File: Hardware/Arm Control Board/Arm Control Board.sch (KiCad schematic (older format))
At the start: 12 parts

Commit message: Added new AP65552SP-13 regulator circuit
More current for the servos
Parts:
- removed 100, C?: CP1, symbol CP1
- removed 3k: R, symbol R
- removed C?: 470 pF, symbol C
- removed D?: 1N5819, symbol DIODESCH
- removed L?: 220 uH, symbol INDUCTOR_SMALL
- removed R?: 1k, symbol R
- removed R?: .33???, symbol R
- removed U?: AZ34063UMTR-G1, symbol AZ34063UMTR-G1
- added C? (x2): 10uF, symbol C
- added C?: .1uF, symbol C
- added C? (x2): 22uF, symbol C
- added C?: 8.2nF, symbol C
- added C?: 1uF, symbol C
- added C?: 18pF, symbol C
- added L?: 3.3uH, symbol INDUCTOR_SMALL
- added P?: BATT, symbol BATT
- added R?: 100K, symbol R
- added R?: 22.1K, symbol R
- added R?: 8.25K, symbol R
- added U?: AP65552SP-13, symbol AP65552SP-13
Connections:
- wire segments 32 -> 38
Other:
- moved on the sheet: P?

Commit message: Creating servo regulator circuits, datasheets
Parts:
- added C? (x2): 10uF, symbol C
- added C?: .1uF, symbol C
- added C? (x2): 22uF, symbol C
- added C?: 8.2nF, symbol C
- added C?: 1uF, symbol C
- added C?: 18pF, symbol C
- added L?: 3.3uH, symbol INDUCTOR_SMALL
- added R?: 100K, symbol R
- added R?: 22.1K, symbol R
- added R?: 8.25K, symbol R
- added U?: AP65552SP-13, symbol AP65552SP-13
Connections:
- wire segments 38 -> 84
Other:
- moved on the sheet: C?, L?, R?, U?

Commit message: Added enable pins to all servo regulators
Might not need them all independent, we'll see
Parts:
- removed C? (x4): 10uF, symbol C
- removed C? (x2): .1uF, symbol C
- removed C? (x4): 22uF, symbol C
- removed C? (x2): 8.2nF, symbol C
- removed C? (x2): 1uF, symbol C
- removed C? (x2): 18pF, symbol C
- removed L? (x2): 3.3uH, symbol INDUCTOR_SMALL
- removed R? (x2): 100K, symbol R
- removed R? (x2): 22.1K, symbol R
- removed R? (x2): 8.25K, symbol R
- removed U? (x2): AP65552SP-13, symbol AP65552SP-13
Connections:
- wire segments 84 -> 8

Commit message: Added and connected servo plugs
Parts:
- added P? (x5): SERVO, symbol SERVO
- added U? (x2): STM32F410RCT6, symbol STM32F410RCT6
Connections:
- wire segments 8 -> 52
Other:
- moved on the sheet: P?, U?A

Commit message: Added lower cost 485 Transceiver, connected serial
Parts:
- removed U?: ST485CDR, symbol ST485CDR
- added U?: SN75176BDR, symbol SN75176BDR
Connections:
- wire segments 52 -> 63
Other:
- moved on the sheet: P?
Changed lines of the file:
@@
-$EndComp
-$Comp
-L ST485CDR U?
-U 1 1 54C4799F
-P 8100 1000
-F 0 "U?" H 7950 550 60  0000 C CNN
-F 1 "ST485CDR" H 7900 1150 60  0000 C CNN
-F 2 "" H 8100 1000 60  0000 C CNN
-F 3 "" H 8100 1000 60  0000 C CNN
-	1    8100 1000
-	1    0    0    -1
 $EndComp
 $Comp
 L RS485 P?
 U 1 1 54C47C8E
-P 9100 1150
-F 0 "P?" H 9100 1300 50  0000 C CNN
-F 1 "RS485" V 9200 1150 50  0000 C CNN
-F 2 "" H 9100 1150 60  0000 C CNN
-F 3 "" H 9100 1150 60  0000 C CNN
-	1    9100 1150
+P 4100 1450
+F 0 "P?" H 4100 1600 50  0000 C CNN
+F 1 "RS485" V 4200 1450 50  0000 C CNN
+F 2 "" H 4100 1450 60  0000 C CNN
+F 3 "" H 4100 1450 60  0000 C CNN
+	1    4100 1450
 	1    0    0    -1
 $EndComp
@@
 L GND #PWR01
 U 1 1 54C47E58
-P 8500 1500
-F 0 "#PWR01" H 8500 1250 60  0001 C CNN
-F 1 "GND" H 8500 1350 60  0000 C CNN
-F 2 "" H 8500 1500 60  0000 C CNN
-F 3 "" H 8500 1500 60  0000 C CNN
-	1    8500 1500
-	1    0    0    -1
-$EndComp
-Wire Wire Line
-	8900 1100 8300 1100
-Wire Wire Line
-	8300 1200 8900 1200
-Wire Wire Line
-	8300 1300 8500 1300
-Wire Wire Line
-	8500 1300 8500 1500
+P 3500 1800
+F 0 "#PWR01" H 3500 1550 60  0001 C CNN
+F 1 "GND" H 3500 1650 60  0000 C CNN
+F 2 "" H 3500 1800 60  0000 C CNN
+F 3 "" H 3500 1800 60  0000 C CNN
+	1    3500 1800
+	1    0    0    -1
+$EndComp
 $Comp
 L BATT P?
@@
 	1    0    0    -1
 $EndComp
-Wire Wire Line
-	850  750  950  750
-Wire Wire Line
-	950  750  950  850
-Wire Wire Line
-	850  650  1200 650
-Wire Wire Line
-	1200 650  1200 850
 $Sheet
 S 4900 3150 1650 1950
@@
 	-1   0    0    1
 $EndComp
-Wire Wire Line
-	4900 3250 2350 3250
-Wire Wire Line
-	4900 3400 4300 3400
-Wire Wire Line
-	4300 3400 4300 3900
-Wire Wire Line
-	4300 3900 2350 3900
-Wire Wire Line
-	4450 3550 4450 4600
-Wire Wire Line
-	4450 4600 2350 4600
-Wire Wire Line
-	4450 3550 4900 3550
-Wire Wire Line
-	4900 3700 4600 3700
-Wire Wire Line
-	4600 3700 4600 5300
-Wire Wire Line
-	4600 5300 2350 5300
-Wire Wire Line
-	4900 3850 4750 3850
-Wire Wire Line
-	4750 3850 4750 6000
-Wire Wire Line
-	4750 6000 2350 6000
 $Comp
 L GND #PWR?
@@
 	1    0    0    -1
 $EndComp
-Wire Wire Line
-	2350 3350 2500 3350
-Wire Wire Line
-	2500 3350 2500 3450
 $Comp
 L GND #PWR?
@@
 	1    0    0    -1
 $EndComp
-Wire Wire Line
-	2350 4000 2500 4000
-Wire Wire Line
-	2500 4000 2500 4100
 $Comp
 L GND #PWR?
@@
 	1    0    0    -1
 $EndComp
-Wire Wire Line
-	2350 4700 2500 4700
-Wire Wire Line
-	2500 4700 2500 4800
 $Comp
 L GND #PWR?
@@
 	1    0    0    -1
 $EndComp
-Wire Wire Line
-	2500 5400 2500 5500
 $Comp
 L GND #PWR?
@@
 	1    0    0    -1
 $EndComp
-Wire Wire Line
-	2350 6100 2500 6100
-Wire Wire Line
-	2500 6100 2500 6200
-Wire Wire Line
-	2500 5400 2350 5400
-Wire Wire Line
-	1400 1850 2650 1850
-Wire Wire Line
-	2650 1850 2650 3150
-Wire Wire Line
-	2650 3150 2350 3150
-Wire Wire Line
-	1400 1950 2750 1950
-Wire Wire Line
-	2750 1950 2750 3800
-Wire Wire Line
-	2750 3800 2350 3800
 $Comp
 L STM32F410RCT6 U?
@@
 	1    0    0    -1
 $EndComp
-Wire Wire Line
-	1400 3000 1900 3000
-Wire Wire Line
-	1900 3000 1900 4400
-Wire Wire Line
-	1900 4400 2500 4400
-Wire Wire Line
-	2500 4400 2500 4500
-Wire Wire Line
-	2500 4500 2350 4500
 $Comp
 L STM32F410RCT6 U?
@@
 $EndComp
 Wire Wire Line
+	3900 1400 3300 1400
+Wire Wire Line
+	3300 1500 3900 1500
+Wire Wire Line
+	3300 1600 3500 1600
+Wire Wire Line
+	3500 1600 3500 1800
+Wire Wire Line
+	850  750  950  750
+Wire Wire Line
+	950  750  950  850
+Wire Wire Line
+	850  650  1200 650
+Wire Wire Line
+	1200 650  1200 850
+Wire Wire Line
+	4900 3250 2350 3250
+Wire Wire Line
+	4900 3400 4300 3400
+Wire Wire Line
+	4300 3400 4300 3900
+Wire Wire Line
+	4300 3900 2350 3900
+Wire Wire Line
+	4450 3550 4450 4600
+Wire Wire Line
+	4450 4600 2350 4600
+Wire Wire Line
+	4450 3550 4900 3550
+Wire Wire Line
+	4900 3700 4600 3700
+Wire Wire Line
+	4600 3700 4600 5300
+Wire Wire Line
+	4600 5300 2350 5300
+Wire Wire Line
+	4900 3850 4750 3850
+Wire Wire Line
+	4750 3850 4750 6000
+Wire Wire Line
+	4750 6000 2350 6000
+Wire Wire Line
+	2350 3350 2500 3350
+Wire Wire Line
+	2500 3350 2500 3450
+Wire Wire Line
+	2350 4000 2500 4000
+Wire Wire Line
+	2500 4000 2500 4100
+Wire Wire Line
+	2350 4700 2500 4700
+Wire Wire Line
+	2500 4700 2500 4800
+Wire Wire Line
+	2500 5400 2500 5500
+Wire Wire Line
+	2350 6100 2500 6100
+Wire Wire Line
+	2500 6100 2500 6200
+Wire Wire Line
+	2500 5400 2350 5400
+Wire Wire Line
+	1400 1850 2650 1850
+Wire Wire Line
+	2650 1850 2650 3150
+Wire Wire Line
+	2650 3150 2350 3150
+Wire Wire Line
+	1400 1950 2750 1950
+Wire Wire Line
+	2750 1950 2750 3800
+Wire Wire Line
+	2750 3800 2350 3800
+Wire Wire Line
+	1400 3000 1900 3000
+Wire Wire Line
+	1900 3000 1900 4400
+Wire Wire Line
+	1900 4400 2500 4400
+Wire Wire Line
+	2500 4400 2500 4500
+Wire Wire Line
+	2500 4500 2350 4500
+Wire Wire Line
 	1400 5550 1900 5550
 Wire Wire Line
@@
 Wire Wire Line
 	2500 5900 2350 5900
+Wire Notes Line
+	7150 6750 7150 6800
+Wire Notes Line
+	7150 6800 7450 6800
+Wire Notes Line
+	7450 6800 7450 6750
+Wire Notes Line
+	7450 6750 7150 6750
+Wire Notes Line
+	7300 6750 7300 6700
+Wire Notes Line
+	7250 6700 7350 6700
+Wire Notes Line
+	7250 6700 7250 6650
+Wire Notes Line
+	7250 6650 7350 6650
+Wire Notes Line
+	7350 6650 7350 6700
+Wire Notes Line
+	7150 6850 7300 6800
+Wire Notes Line
+	7150 6850 7100 6850
+Wire Notes Line
+	7150 6850 7150 6900
+Wire Notes Line
+	7150 6900 7100 6900
+Wire Notes Line
+	7100 6900 7100 6850
+Wire Notes Line
+	7500 6850 7450 6850
+Wire Notes Line
+	7450 6850 7450 6900
+Wire Notes Line
+	7450 6900 7500 6900
+Wire Notes Line
+	7500 6900 7500 6850
+Wire Notes Line
+	7250 6850 7300 6850
+Wire Notes Line
+	7250 6850 7250 6900
+Wire Notes Line
+	7250 6900 7300 6900
+Wire Notes Line
+	7300 6900 7300 6850
+Wire Notes Line
+	7500 6850 7300 6800
+Wire Notes Line
+	7250 6850 7400 6825
+$Comp
+L SN75176BDR U?
+U 1 1 54C9A1F6
+P 3100 1300
+F 0 "U?" H 2950 850 60  0000 C CNN
+F 1 "SN75176BDR" H 2900 1450 60  0000 C CNN
+F 2 "" H 3100 1300 60  0000 C CNN
+F 3 "" H 3100 1300 60  0000 C CNN
+	1    3100 1300
+	1    0    0    -1
+$EndComp
+Wire Wire Line
+	2550 1600 2000 1600
+Wire Wire Line
+	2000 1600 2000 2150
+Wire Wire Line
+	2000 2150 1400 2150
+Wire Wire Line
+	1900 1300 1900 2250
+Wire Wire Line
+	1900 2250 1400 2250
+Wire Wire Line
+	1900 1300 2550 1300
+Wire Wire Line
+	2550 1500 1800 1500
+Wire Wire Line
+	1800 1500 1800 2050
+Wire Wire Line
+	1800 2050 1400 2050
+Wire Wire Line
+	2550 1400 2050 1400
+Wire Wire Line
+	2050 1400 2050 1500
+Connection ~ 2050 1500
 $EndSCHEMATC

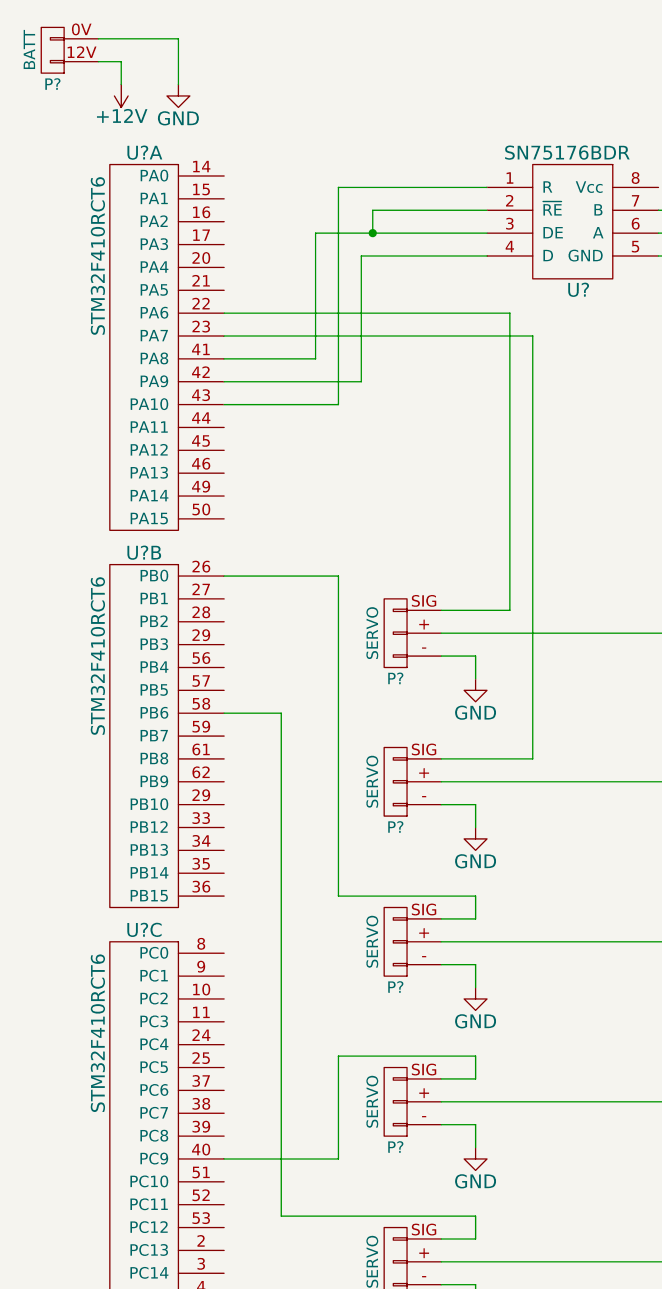
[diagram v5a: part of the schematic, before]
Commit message: Added SyRen serial connector
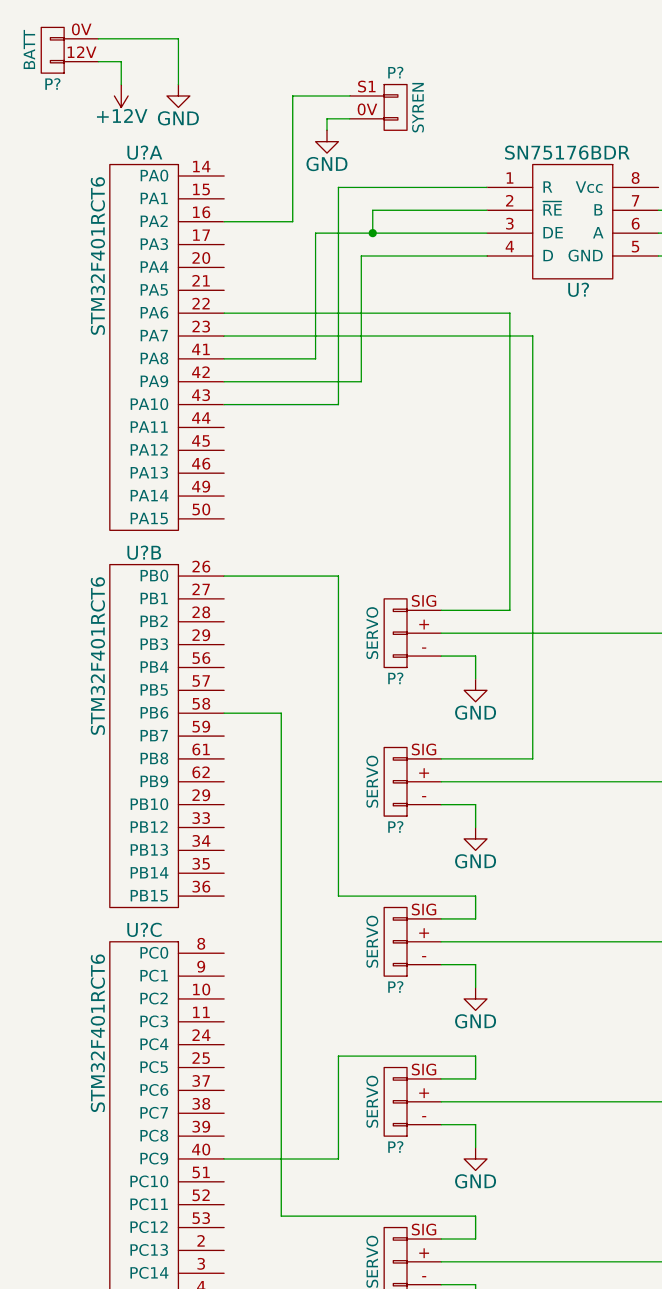
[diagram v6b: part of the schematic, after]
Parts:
- removed U? (x3): STM32F410RCT6, symbol STM32F410RCT6
- added P?: SYREN, symbol SYREN
- added U? (x3): STM32F401RCT6, symbol STM32F401RCT6
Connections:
- net GND: now also P?.0V
- net at P?.SIG: now also U?.22 (PA6)
- net at P?.SIG: now also U?.23 (PA7)
- net at U?.2 (~RE), U?.3 (DE): now also U?.41 (PA8)
- net at U?.4 (D): now also U?.42 (PA9)
- net at U?.1 (R): now also U?.43 (PA10)
- net at P?.SIG: now also U?.26 (PB0)
- net at P?.SIG: now also U?.40 (PC9)
- net at P?.SIG: now also U?.58 (PB6)
- new net: P?.S1, U?.16 (PA2)
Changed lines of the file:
@@
 $EndDescr
-$Comp
-L STM32F410RCT6 U?
-U 1 1 54C46252
-P 1200 1250
-F 0 "U?" H 1050 1350 60  0000 C CNN
-F 1 "STM32F410RCT6" V 850 900 60  0000 C CNN
-F 2 "" H 1200 -250 60  0000 C CNN
-F 3 "" H 1200 -250 60  0000 C CNN
-	1    1200 1250
-	1    0    0    -1
-$EndComp
 $Comp
 L RS485 P?
@@
 	1    0    0    -1
 $EndComp
-$Comp
-L STM32F410RCT6 U?
-U 2 1 54C8CAE9
-P 1200 3000
-F 0 "U?" H 1050 3100 60  0000 C CNN
-F 1 "STM32F410RCT6" V 850 2650 60  0000 C CNN
-F 2 "" H 1200 1400 60  0000 C CNN
-F 3 "" H 1200 1400 60  0000 C CNN
-	2    1200 3000
-	1    0    0    -1
-$EndComp
-$Comp
-L STM32F410RCT6 U?
-U 3 1 54C8E524
-P 1200 4650
-F 0 "U?" H 1050 4750 60  0000 C CNN
-F 1 "STM32F410RCT6" V 850 4300 60  0000 C CNN
-F 2 "" H 1200 3050 60  0000 C CNN
-F 3 "" H 1200 3050 60  0000 C CNN
-	3    1200 4650
-	1    0    0    -1
-$EndComp
 Wire Wire Line
 	3900 1400 3300 1400
@@
 	2050 1400 2050 1500
 Connection ~ 2050 1500
+Wire Wire Line
+	1400 1450 1700 1450
+Wire Wire Line
+	1700 1450 1700 900
+Wire Wire Line
+	1700 900  1950 900
+$Comp
+L STM32F401RCT6 U?
+U 1 1 54C9C8AC
+P 1200 1250
+F 0 "U?" H 1050 1350 60  0000 C CNN
+F 1 "STM32F401RCT6" V 850 900 60  0000 C CNN
+F 2 "" H 1200 -350 60  0000 C CNN
+F 3 "" H 1200 -350 60  0000 C CNN
+	1    1200 1250
+	1    0    0    -1
+$EndComp
+$Comp
+L STM32F401RCT6 U?
+U 2 1 54C9CF17
+P 1200 3000
+F 0 "U?" H 1050 3100 60  0000 C CNN
+F 1 "STM32F401RCT6" V 850 2650 60  0000 C CNN
+F 2 "" H 1200 1400 60  0000 C CNN
+F 3 "" H 1200 1400 60  0000 C CNN
+	2    1200 3000
+	1    0    0    -1
+$EndComp
+$Comp
+L STM32F401RCT6 U?
+U 3 1 54C9D282
+P 1200 4650
+F 0 "U?" H 1050 4750 60  0000 C CNN
+F 1 "STM32F401RCT6" V 850 4300 60  0000 C CNN
+F 2 "" H 1200 3050 60  0000 C CNN
+F 3 "" H 1200 3050 60  0000 C CNN
+	3    1200 4650
+	1    0    0    -1
+$EndComp
+$Comp
+L SYREN P?
+U 1 1 54C9E181
+P 2150 950
+F 0 "P?" H 2150 1100 50  0000 C CNN
+F 1 "SYREN" V 2250 950 50  0000 C CNN
+F 2 "" H 2150 950 60  0000 C CNN
+F 3 "" H 2150 950 60  0000 C CNN
+	1    2150 950
+	1    0    0    -1
+$EndComp
+$Comp
+L GND #PWR?
+U 1 1 54C9E250
+P 1850 1050
+F 0 "#PWR?" H 1850 800 60  0001 C CNN
+F 1 "GND" H 1850 900 60  0000 C CNN
+F 2 "" H 1850 1050 60  0000 C CNN
+F 3 "" H 1850 1050 60  0000 C CNN
+	1    1850 1050
+	1    0    0    -1
+$EndComp
+Wire Wire Line
+	1950 1000 1850 1000
+Wire Wire Line
+	1850 1000 1850 1050
 $EndSCHEMATC

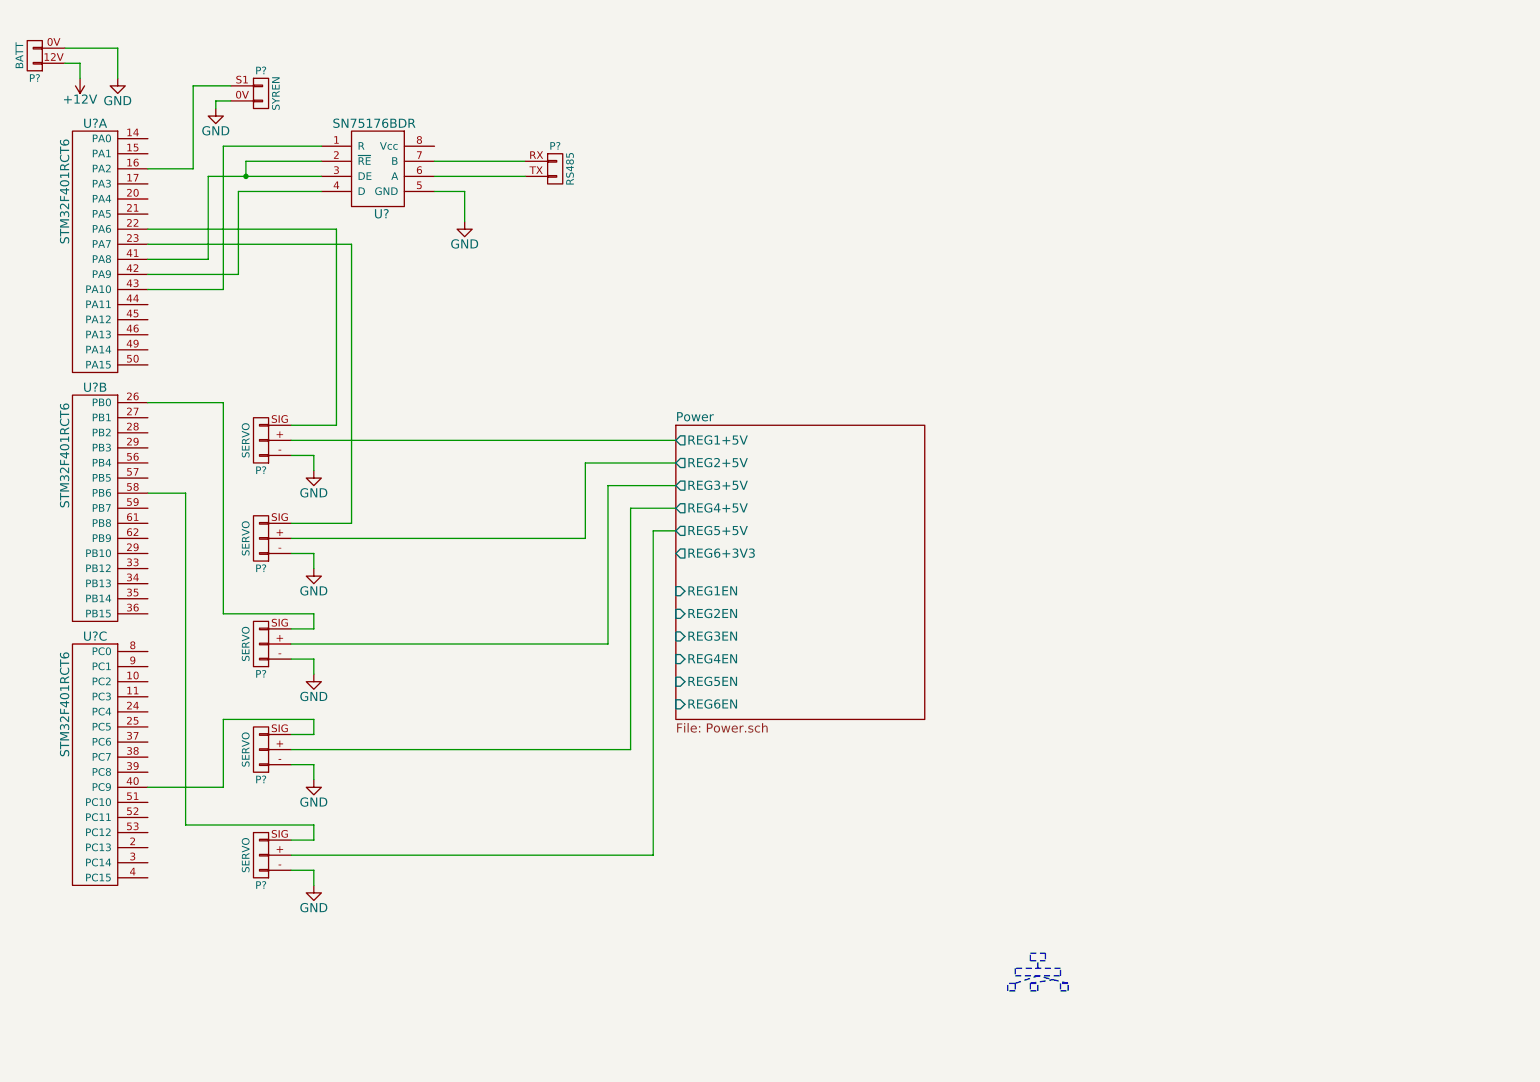
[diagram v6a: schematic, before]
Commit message: Raspberry Pi power connector + started STM32 power
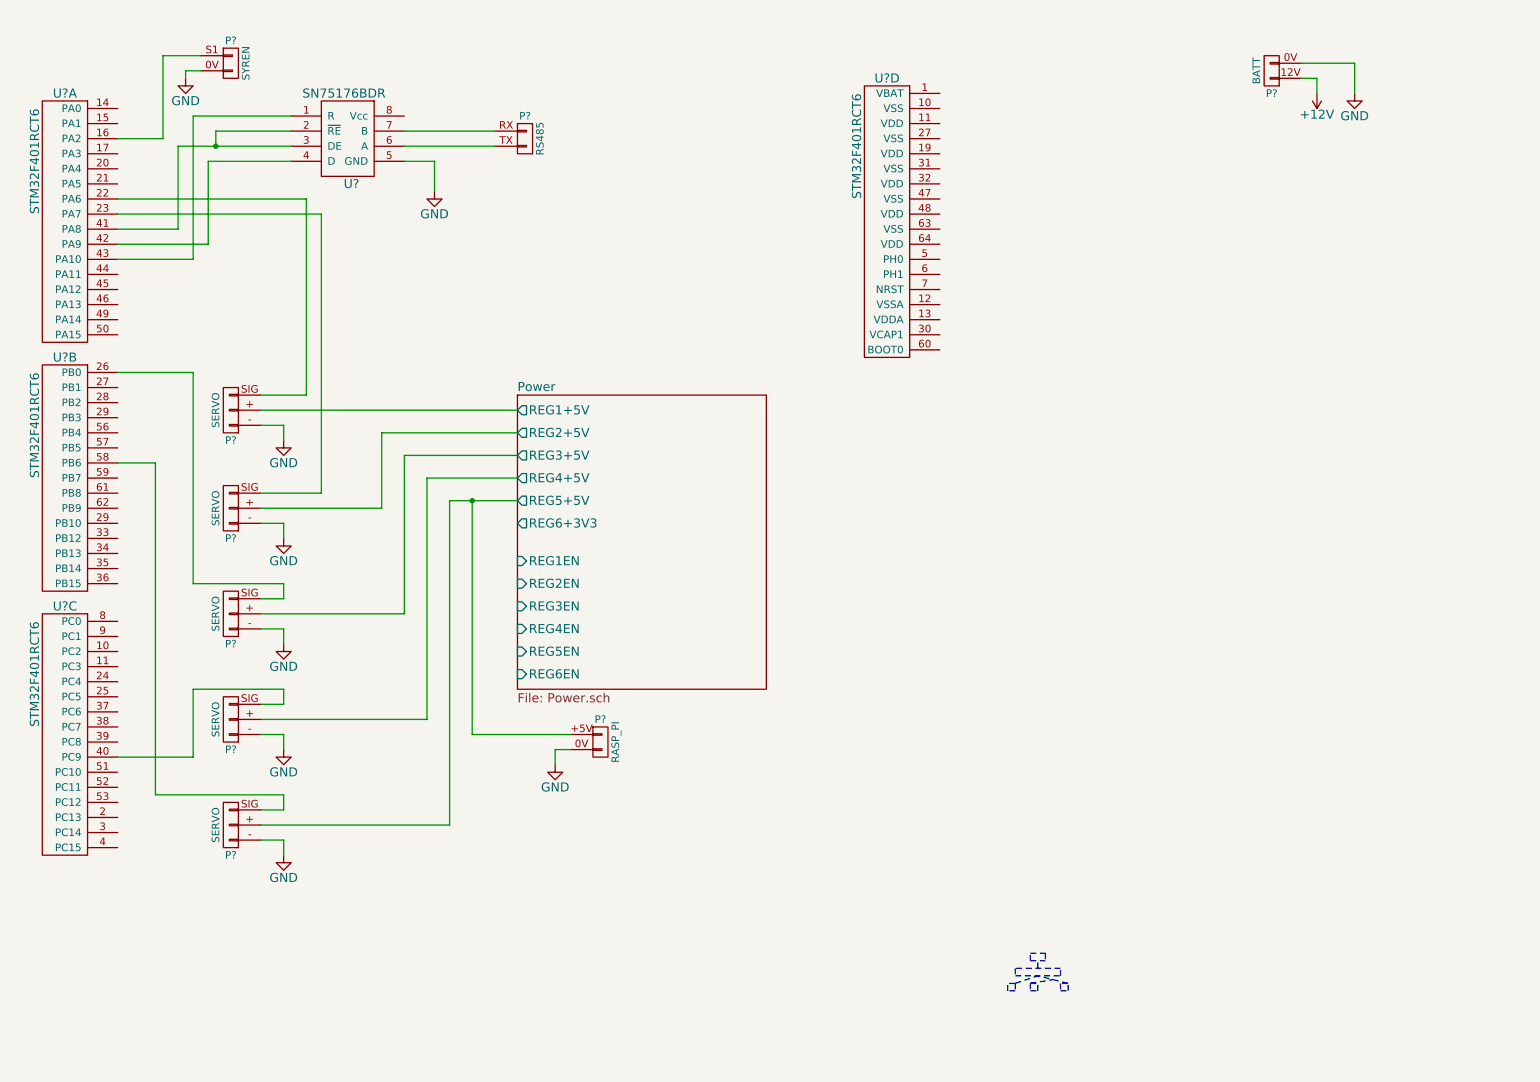
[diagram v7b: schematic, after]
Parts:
- added P?: RASP_PI, symbol RASP_PI
- added U?: STM32F401RCT6, symbol STM32F401RCT6
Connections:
- net GND: now also P?.0V
- net Power/REG5+5V: now also P?.+5V
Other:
- moved on the sheet: P?, U?, U?A, U?B, U?C
